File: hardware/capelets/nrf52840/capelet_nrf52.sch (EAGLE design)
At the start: 2 parts

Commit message: hardware: updated capelets
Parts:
- added LED1: 598-8130-107FLED_0805, shepherd:598-8130-107FLED_0805
- added R1: 100R, shepherd:R_SMD0805
- added R2: 10k, shepherd:R_SMD0805
- added R3: 50R, shepherd:R_SMD0805
- added T1: SI2374DSSOT23-VSHAY, shepherd:SI2374DSSOT23-VSHAY
- U$1: value SHPRD_CPLT_T -> SHPRD_CPLT_NRF52; device mylib:SHPRD_CPLT_T -> shepherd:SHPRD_CPLT_NRF52
- U$2: device mylib:NRF52840-DONGLE -> shepherd:NRF52840-DONGLE
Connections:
- new net GPIO_LED: R2.1, R3.1, U$2.P0.02
- new net N$1: R3.2, T1.G
- new net N$3: LED1.C, T1.D
- new net N$4: LED1.A, R1.1
- net GND: now also R2.2, T1.S
- net V_SUP: now also R1.2
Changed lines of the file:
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@@
 <?xml version="1.0" encoding="utf-8"?>
 <!DOCTYPE eagle SYSTEM "eagle.dtd">
-<eagle version="9.2.2">
+<eagle version="9.4.2">
 <drawing>
 <settings>
@@
 <layer number="112" name="tSilk" color="7" fill="1" visible="no" active="yes"/>
 <layer number="113" name="ReferenceLS" color="7" fill="1" visible="no" active="no"/>
+<layer number="114" name="ANT" color="7" fill="1" visible="no" active="yes"/>
+<layer number="115" name="usb" color="7" fill="1" visible="no" active="yes"/>
 <layer number="116" name="Patch_BOT" color="9" fill="4" visible="no" active="yes"/>
 <layer number="118" name="Rect_Pads" color="7" fill="1" visible="no" active="no"/>
@@
 <layer number="132" name="bAdjust" color="7" fill="1" visible="no" active="yes"/>
 <layer number="144" name="Drill_legend" color="7" fill="1" visible="no" active="yes"/>
+<layer number="145" name="DrillLegend_01-02" color="7" fill="1" visible="no" active="yes"/>
+<layer number="146" name="DrillLegend_01-15" color="7" fill="1" visible="no" active="yes"/>
+<layer number="147" name="DrillLegend_01-16" color="7" fill="1" visible="no" active="yes"/>
+<layer number="148" name="DrillLegend_01-20" color="7" fill="1" visible="no" active="yes"/>
+<layer number="149" name="DrillLegend_02-15" color="7" fill="1" visible="no" active="yes"/>
 <layer number="150" name="Notes" color="7" fill="1" visible="no" active="yes"/>
 <layer number="151" name="HeatSink" color="7" fill="1" visible="no" active="yes"/>
@@
 </classes>
 <parts>
-<part name="U$1" library="mylib" deviceset="SHPRD_CPLT_T" device=""/>
-<part name="U$2" library="mylib" deviceset="NRF52840-DONGLE" device=""/>
+<part name="U$1" library="shepherd" deviceset="SHPRD_CPLT_NRF52" device=""/>
+<part name="U$2" library="shepherd" deviceset="NRF52840-DONGLE" device=""/>
 <part name="GND1" library="supply1" library_urn="urn:adsk.eagle:library:371" deviceset="GND" device=""/>
 <part name="GND2" library="supply1" library_urn="urn:adsk.eagle:library:371" deviceset="GND" device=""/>
 <part name="GND3" library="supply1" library_urn="urn:adsk.eagle:library:371" deviceset="GND" device=""/>
 <part name="GND4" library="supply1" library_urn="urn:adsk.eagle:library:371" deviceset="GND" device=""/>
+<part name="R1" library="shepherd" deviceset="R_SMD" device="0805" value="100R"/>
+<part name="LED1" library="shepherd" deviceset="598-8130-107F" device="LED_0805" package3d_urn="urn:adsk.eagle:package:5033917/1"/>
+<part name="T1" library="shepherd" deviceset="SI2374DS" device="SOT23-VSHAY" package3d_urn="urn:adsk.eagle:package:5032659/1"/>
+<part name="GND5" library="supply1" library_urn="urn:adsk.eagle:library:371" deviceset="GND" device=""/>
+<part name="R2" library="shepherd" deviceset="R_SMD" device="0805" value="10k"/>
+<part name="R3" library="shepherd" deviceset="R_SMD" device="0805" value="50R"/>
 </parts>
 <sheets>
@@
 <attribute name="VALUE" x="53.34" y="-5.08" size="1.778" layer="96"/>
 </instance>
-<instance part="GND3" gate="1" x="104.14" y="-2.54" smashed="yes">
-<attribute name="VALUE" x="101.6" y="-5.08" size="1.778" layer="96"/>
-</instance>
-<instance part="GND4" gate="1" x="147.32" y="-2.54" smashed="yes">
-<attribute name="VALUE" x="144.78" y="-5.08" size="1.778" layer="96"/>
+<instance part="GND3" gate="1" x="101.6" y="-7.62" smashed="yes">
+<attribute name="VALUE" x="99.06" y="-10.16" size="1.778" layer="96"/>
+</instance>
+<instance part="GND4" gate="1" x="147.32" y="-7.62" smashed="yes">
+<attribute name="VALUE" x="144.78" y="-10.16" size="1.778" layer="96"/>
+</instance>
+<instance part="R1" gate="G$1" x="208.28" y="38.1" smashed="yes" rot="R90">
+<attribute name="NAME" x="206.7814" y="34.29" size="1.778" layer="95" rot="R90"/>
+<attribute name="VALUE" x="211.582" y="34.29" size="1.778" layer="96" rot="R90"/>
+</instance>
+<instance part="LED1" gate="A" x="208.28" y="27.94" smashed="yes">
+<attribute name="NAME" x="211.836" y="23.368" size="1.778" layer="95" rot="R90"/>
+</instance>
+<instance part="T1" gate="G$1" x="205.74" y="15.24" smashed="yes">
+<attribute name="VALUE" x="194.31" y="15.24" size="1.778" layer="96"/>
+<attribute name="NAME" x="194.31" y="17.78" size="1.778" layer="95"/>
+</instance>
+<instance part="GND5" gate="1" x="208.28" y="-7.62" smashed="yes">
+<attribute name="VALUE" x="205.74" y="-10.16" size="1.778" layer="96"/>
+</instance>
+<instance part="R2" gate="G$1" x="187.96" y="5.08" smashed="yes" rot="R270">
+<attribute name="NAME" x="189.4586" y="8.89" size="1.778" layer="95" rot="R270"/>
+<attribute name="VALUE" x="184.658" y="8.89" size="1.778" layer="96" rot="R270"/>
+</instance>
+<instance part="R3" gate="G$1" x="195.58" y="12.7" smashed="yes">
+<attribute name="NAME" x="191.77" y="14.1986" size="1.778" layer="95"/>
+<attribute name="VALUE" x="191.77" y="9.398" size="1.778" layer="96"/>
 </instance>
 </instances>
@@
 <segment>
 <pinref part="U$2" gate="G$1" pin="VDDOUT"/>
-<wire x1="144.78" y1="43.18" x2="147.32" y2="43.18" width="0.1524" layer="91"/>
-<label x="147.32" y="43.18" size="1.778" layer="95" xref="yes"/>
+<wire x1="144.78" y1="43.18" x2="152.4" y2="43.18" width="0.1524" layer="91"/>
+<label x="152.4" y="43.18" size="1.778" layer="95" xref="yes"/>
+</segment>
+<segment>
+<pinref part="R1" gate="G$1" pin="2"/>
+<wire x1="208.28" y1="43.18" x2="208.28" y2="48.26" width="0.1524" layer="91"/>
+<label x="208.28" y="48.26" size="1.778" layer="95" rot="R90" xref="yes"/>
 </segment>
 </net>
@@
 <segment>
 <pinref part="U$2" gate="G$1" pin="SWDCLK"/>
-<wire x1="144.78" y1="53.34" x2="147.32" y2="53.34" width="0.1524" layer="91"/>
-<label x="147.32" y="53.34" size="1.778" layer="95" xref="yes"/>
+<wire x1="144.78" y1="53.34" x2="152.4" y2="53.34" width="0.1524" layer="91"/>
+<label x="152.4" y="53.34" size="1.778" layer="95" xref="yes"/>
 </segment>
 <segment>
@@
 <pinref part="GND3" gate="1" pin="GND"/>
 <pinref part="U$2" gate="G$1" pin="GND@1"/>
-<wire x1="104.14" y1="0" x2="104.14" y2="2.54" width="0.1524" layer="91"/>
-<wire x1="104.14" y1="2.54" x2="106.68" y2="2.54" width="0.1524" layer="91"/>
+<wire x1="101.6" y1="-5.08" x2="101.6" y2="2.54" width="0.1524" layer="91"/>
+<wire x1="101.6" y1="2.54" x2="106.68" y2="2.54" width="0.1524" layer="91"/>
 </segment>
 <segment>
 <pinref part="GND4" gate="1" pin="GND"/>
 <pinref part="U$2" gate="G$1" pin="GND@2"/>
-<wire x1="147.32" y1="0" x2="147.32" y2="2.54" width="0.1524" layer="91"/>
+<wire x1="147.32" y1="-5.08" x2="147.32" y2="2.54" width="0.1524" layer="91"/>
 <wire x1="147.32" y1="2.54" x2="144.78" y2="2.54" width="0.1524" layer="91"/>
+</segment>
+<segment>
+<pinref part="R2" gate="G$1" pin="2"/>
+<wire x1="187.96" y1="0" x2="187.96" y2="-2.54" width="0.1524" layer="91"/>
+<wire x1="187.96" y1="-2.54" x2="208.28" y2="-2.54" width="0.1524" layer="91"/>
+<pinref part="T1" gate="G$1" pin="S"/>
+<wire x1="208.28" y1="-2.54" x2="208.28" y2="10.16" width="0.1524" layer="91"/>
+<pinref part="GND5" gate="1" pin="GND"/>
+<wire x1="208.28" y1="-2.54" x2="208.28" y2="-5.08" width="0.1524" layer="91"/>
+<junction x="208.28" y="-2.54"/>
+</segment>
+</net>
+<net name="N$1" class="0">
+<segment>
+<pinref part="T1" gate="G$1" pin="G"/>
+<wire x1="203.2" y1="12.7" x2="200.66" y2="12.7" width="0.1524" layer="91"/>
+<pinref part="R3" gate="G$1" pin="2"/>
+</segment>
+</net>
+<net name="N$3" class="0">
+<segment>
+<pinref part="T1" gate="G$1" pin="D"/>
+<pinref part="LED1" gate="A" pin="C"/>
+<wire x1="208.28" y1="20.32" x2="208.28" y2="22.86" width="0.1524" layer="91"/>
+</segment>
+</net>
+<net name="N$4" class="0">
+<segment>
+<pinref part="LED1" gate="A" pin="A"/>
+<pinref part="R1" gate="G$1" pin="1"/>
+<wire x1="208.28" y1="30.48" x2="208.28" y2="33.02" width="0.1524" layer="91"/>
+</segment>
+</net>
+<net name="GPIO_LED" class="0">
+<segment>
+<pinref part="R2" gate="G$1" pin="1"/>
+<wire x1="187.96" y1="10.16" x2="187.96" y2="12.7" width="0.1524" layer="91"/>
+<pinref part="R3" gate="G$1" pin="1"/>
+<wire x1="187.96" y1="12.7" x2="190.5" y2="12.7" width="0.1524" layer="91"/>
+<wire x1="187.96" y1="12.7" x2="185.42" y2="12.7" width="0.1524" layer="91"/>
+<junction x="187.96" y="12.7"/>
+<label x="185.42" y="12.7" size="1.778" layer="95" rot="R180" xref="yes"/>
+</segment>
+<segment>
+<pinref part="U$2" gate="G$1" pin="P0.02"/>
+<wire x1="144.78" y1="22.86" x2="152.4" y2="22.86" width="0.1524" layer="91"/>
+<label x="152.4" y="22.86" size="1.778" layer="95" xref="yes"/>
 </segment>
 </net>
@@
 will not be understood (or retained) with this version.
 </note>
+<note version="8.3" severity="warning">
+Since Version 8.3, EAGLE supports the association of 3D packages
+with devices in libraries, schematics, and board files. Those 3D
+packages will not be understood (or retained) with this version.
+</note>
 </compatibility>

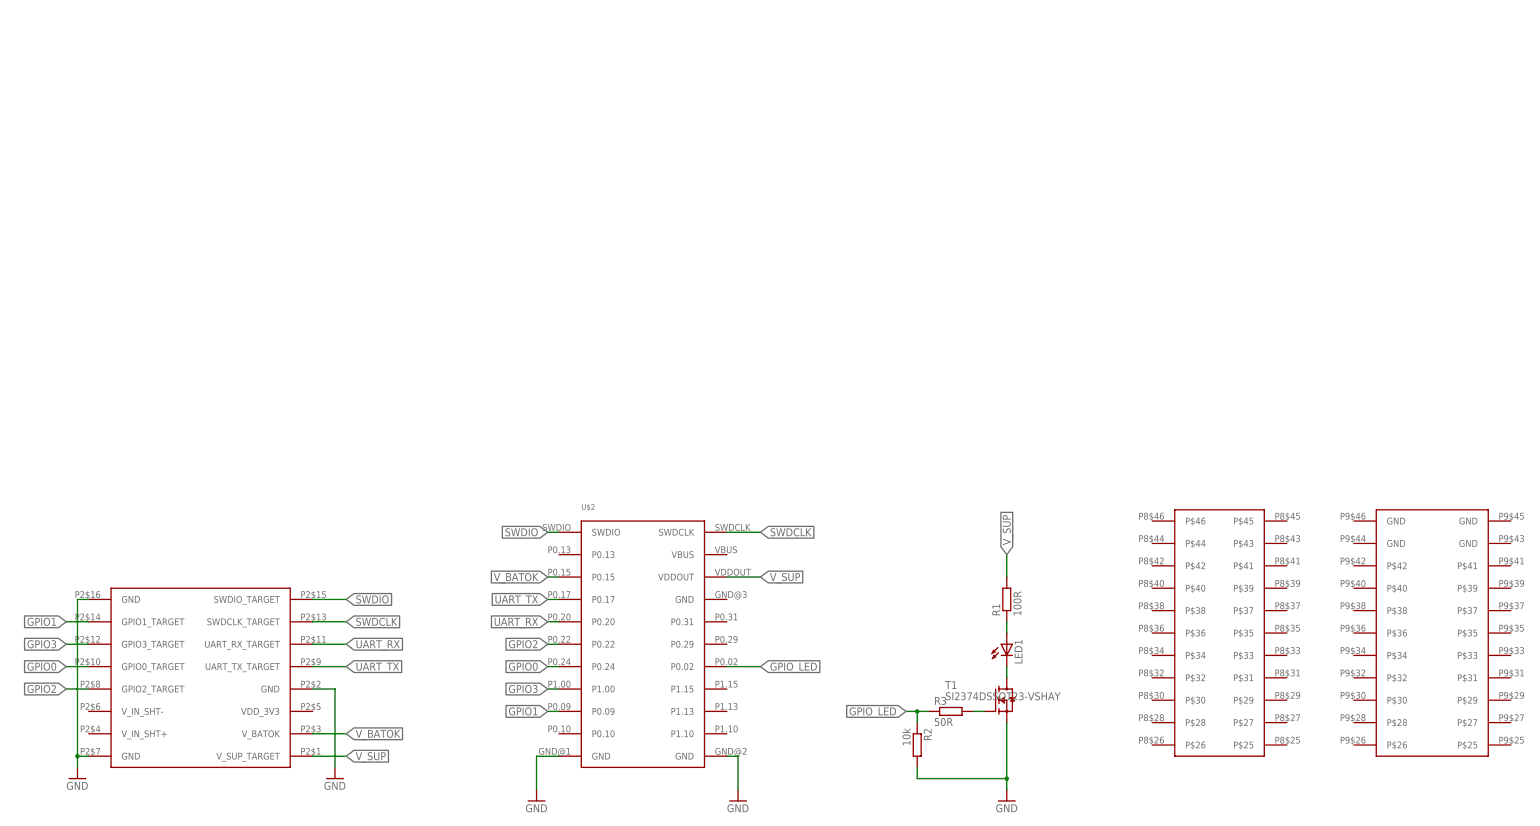
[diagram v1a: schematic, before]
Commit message: hardware: fancy frames around capelet schematics
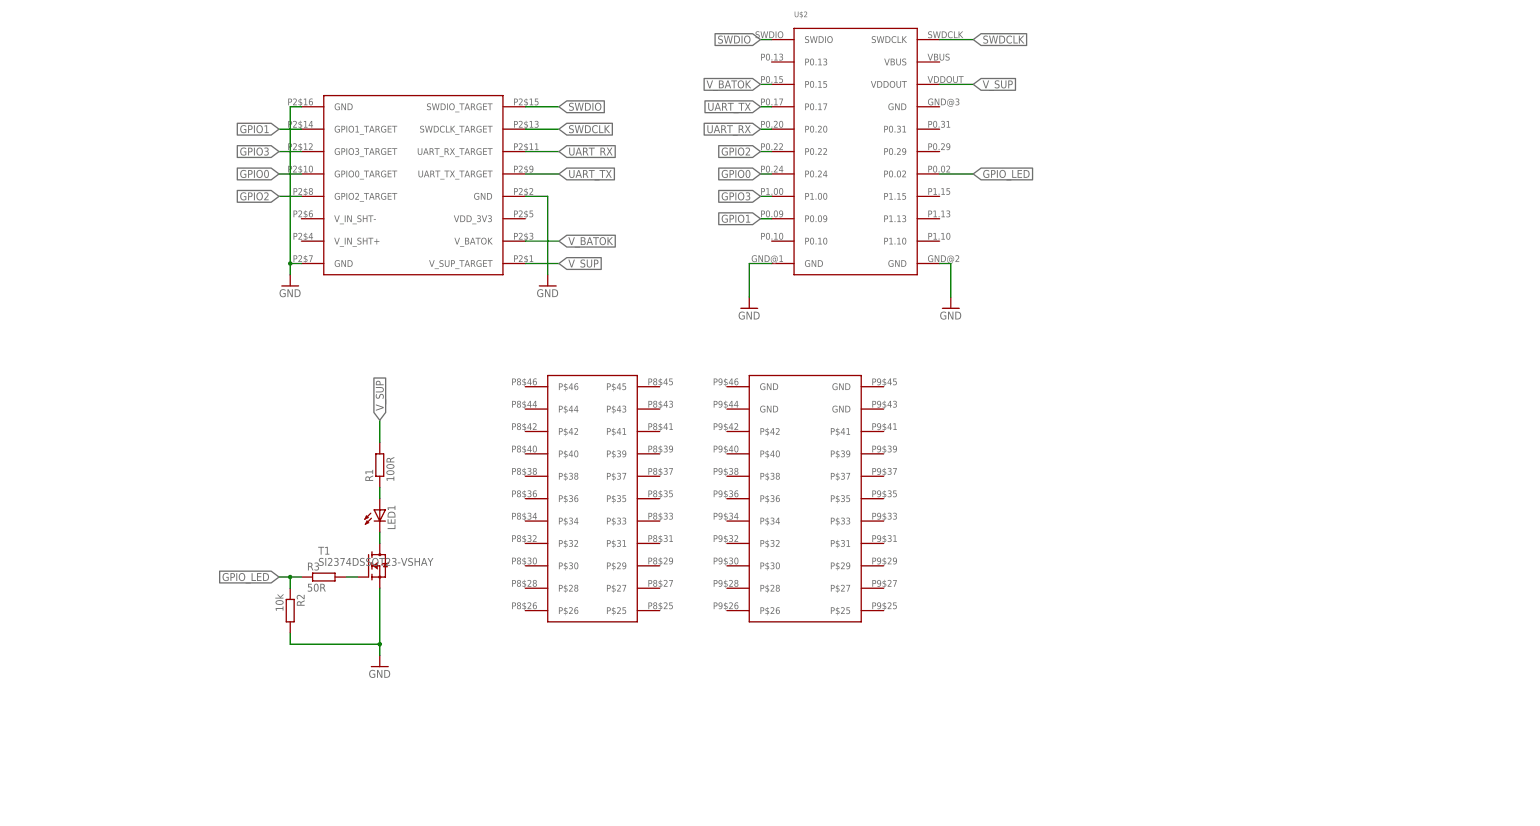
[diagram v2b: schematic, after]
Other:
- moved on the sheet: LED1, R1, R2, R3, T1, U$2

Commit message: hardware: prepared capelets for external manufacturing
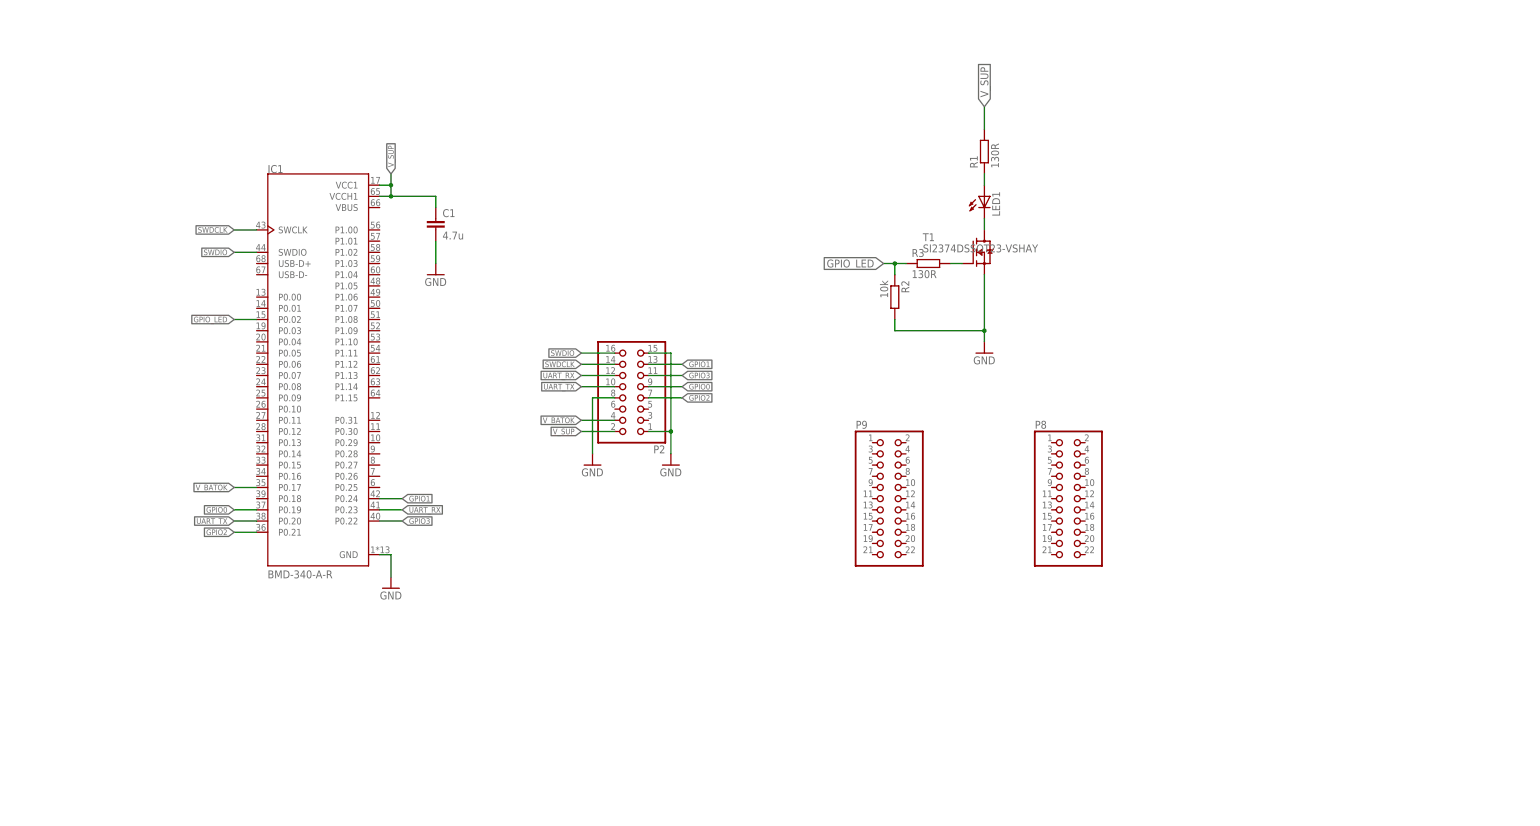
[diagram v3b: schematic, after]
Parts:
- removed U$1: SHPRD_CPLT_NRF52, shepherd:SHPRD_CPLT_NRF52
- removed U$2: NRF52840-DONGLE, shepherd:NRF52840-DONGLE
- added C1: 4.7u, shepherd:C_SMD0603
- added IC1: BMD-340-A-R, shepherd:BMD-340-A-R
- added P2: (no value), pinhead:PINHD-2X8
- added P8, P9: (no value), pinhead:PINHD-2X11
- R1: value 100R -> 130R
- R3: value 50R -> 130R
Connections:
- net GND: now also C1.2, IC1.GND, P2.1, P2.15, P2.8; no longer U$1G$1.GND@2, U$1G$1.GND@3, U$1G$1.GND@4, U$2.GND@1, U$2.GND@2
- net GPIO0: now also IC1.P0.19, P2.9; no longer U$1G$1.GPIO0_TARGET, U$2.P0.24
- net GPIO1: now also IC1.P0.24, P2.13; no longer U$1G$1.GPIO1_TARGET, U$2.P0.09
- net GPIO2: now also IC1.P0.21, P2.7; no longer U$1G$1.GPIO2_TARGET, U$2.P0.22
- net GPIO3: now also IC1.P0.22, P2.11; no longer U$1G$1.GPIO3_TARGET, U$2.P1.00
- net GPIO_LED: now also IC1.P0.02; no longer U$2.P0.02
- net SWDCLK: now also IC1.SWCLK, P2.14; no longer U$1G$1.SWDCLK_TARGET, U$2.SWDCLK
- net SWDIO: now also IC1.SWDIO, P2.16; no longer U$1G$1.SWDIO_TARGET, U$2.SWDIO
- net UART_RX: now also IC1.P0.23, P2.12; no longer U$1G$1.UART_RX_TARGET, U$2.P0.20
- net UART_TX: now also IC1.P0.20, P2.10; no longer U$1G$1.UART_TX_TARGET, U$2.P0.17
- net V_BATOK: now also IC1.P0.17, P2.4; no longer U$1G$1.V_BATOK, U$2.P0.15
- net V_SUP: now also C1.1, IC1.VCC1, IC1.VCCH1, P2.2; no longer U$1G$1.V_SUP_TARGET, U$2.VDDOUT
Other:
- moved on the sheet: LED1, R1, R2, R3, T1
